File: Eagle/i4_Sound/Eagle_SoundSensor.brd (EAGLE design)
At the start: 20 x 23.8 mm, 20 parts, among them U1 LM358DR

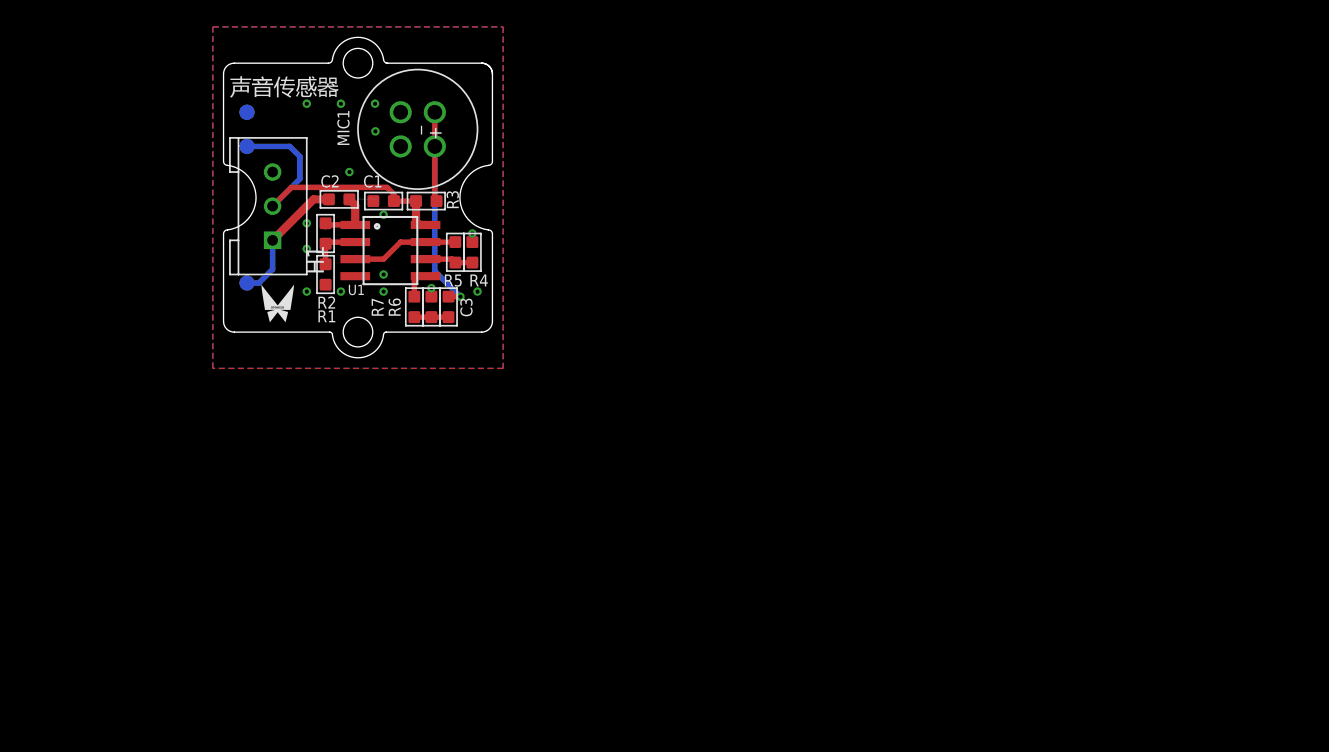
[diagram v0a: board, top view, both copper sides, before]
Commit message: 调整蜂鸣器
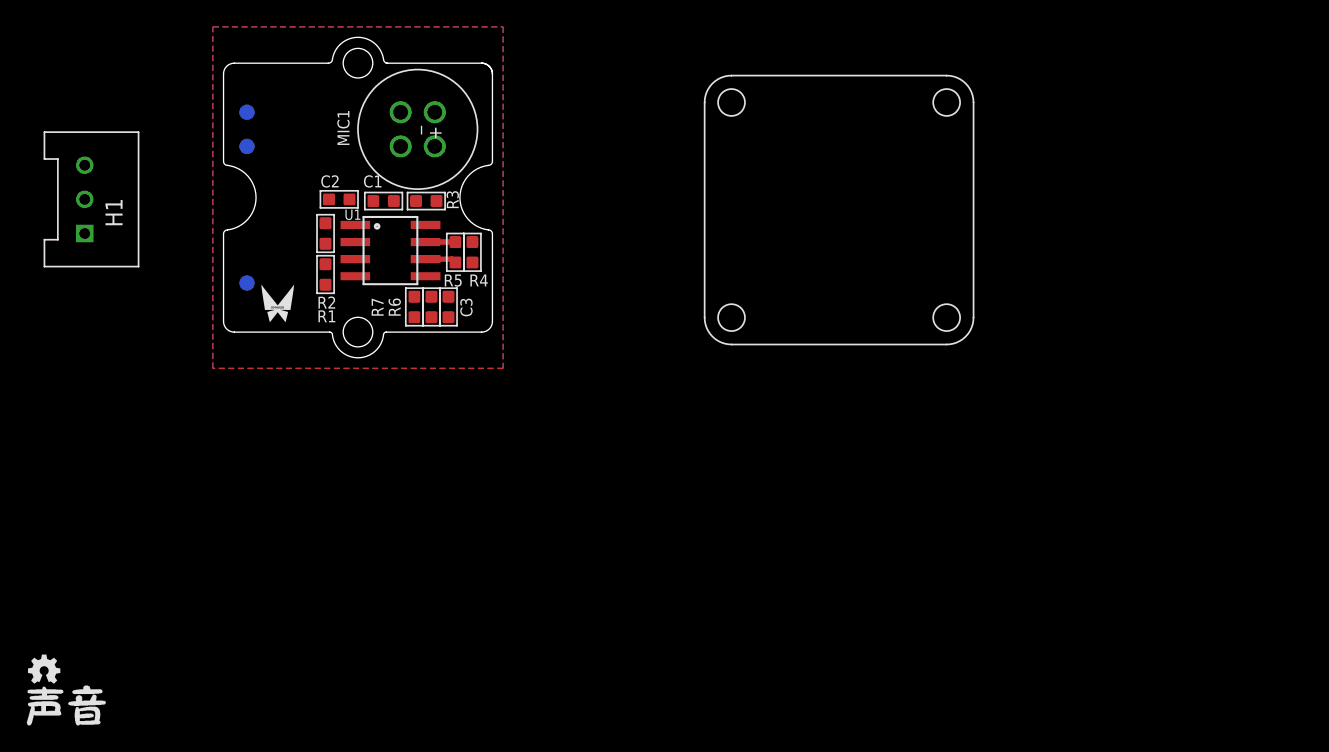
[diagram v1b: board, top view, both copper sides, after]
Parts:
- added U$11: DIMENSION_2MM2MM, Xmaker:DIMENSION_2MM*2MM
- added U$12: OPENHARDWARE_2.5MM_TOP, Xmaker:OPENSOURCELOGO_2.5MM
- added U$13: NAME_SOUND, Xmaker:NAME_SOUND
- H1: value HEAD_LOCK -> HEAD_LOCK_3PIN_2; device HEAD_LOCK:HEAD_LOCK -> Xmaker:HEAD_LOCK_3PIN_2
- moved H1 14.3 mm to (-20.3, -0.13), turned to 180 degrees
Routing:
- net VCC: track 23.1 -> 0.00 mm
- net N$7: track 19.5 -> 0.18 mm, vias 1 -> 0
- net OUT: track 9.94 -> 0.00 mm
- net N$12: track 7.97 -> 2.21 mm
- net OUT1: track 4.60 -> 0.25 mm
- net N$16: track 3.79 -> 0.00 mm
- net N$3: track 2.54 -> 0.00 mm
- net N$1: track 2.21 -> 0.00 mm
- net N$2: track 3.59 -> 2.32 mm
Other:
- board text removed: "C:/Users/Xiangzi/Desktop/Ãû³Æ/Sound.bmp"
- board text removed: "GND"
- board text removed: "SIG"
- board text removed: "VCC"

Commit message: light
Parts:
- moved C1 26.9 mm to (26.3, -11.7)
- moved C3 26.9 mm to (31.1, -19.6)
- moved GND 26.9 mm to (16.1, -5.08)
- moved H1 26.9 mm to (4.06, -11.6)
- moved MIC1 26.9 mm to (28.8, -6.35)
- moved MIC2 26.9 mm to (28.8, -6.35)
- moved OUT 26.9 mm to (16.1, -17.8)
- moved R1 26.9 mm to (22.0, -17.1)
- moved R2 26.9 mm to (22.0, -14.1)
- moved R3 26.9 mm to (29.5, -11.7)
- moved R4 26.9 mm to (32.9, -15.5)
- moved R5 26.9 mm to (31.6, -15.5)
- moved R6 26.9 mm to (29.8, -19.6)
- moved R7 26.9 mm to (28.6, -19.6)
- moved U$1 26.9 mm to (32.6, -17.1)
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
